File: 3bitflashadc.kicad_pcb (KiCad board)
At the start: 2 copper layers, 118.1 x 88.9 mm, 42 parts, among them J1 ExternalPower, U1 LM339, U2 LM339, U3 LM339, U4 74LS04, U5 7447, U6 74147

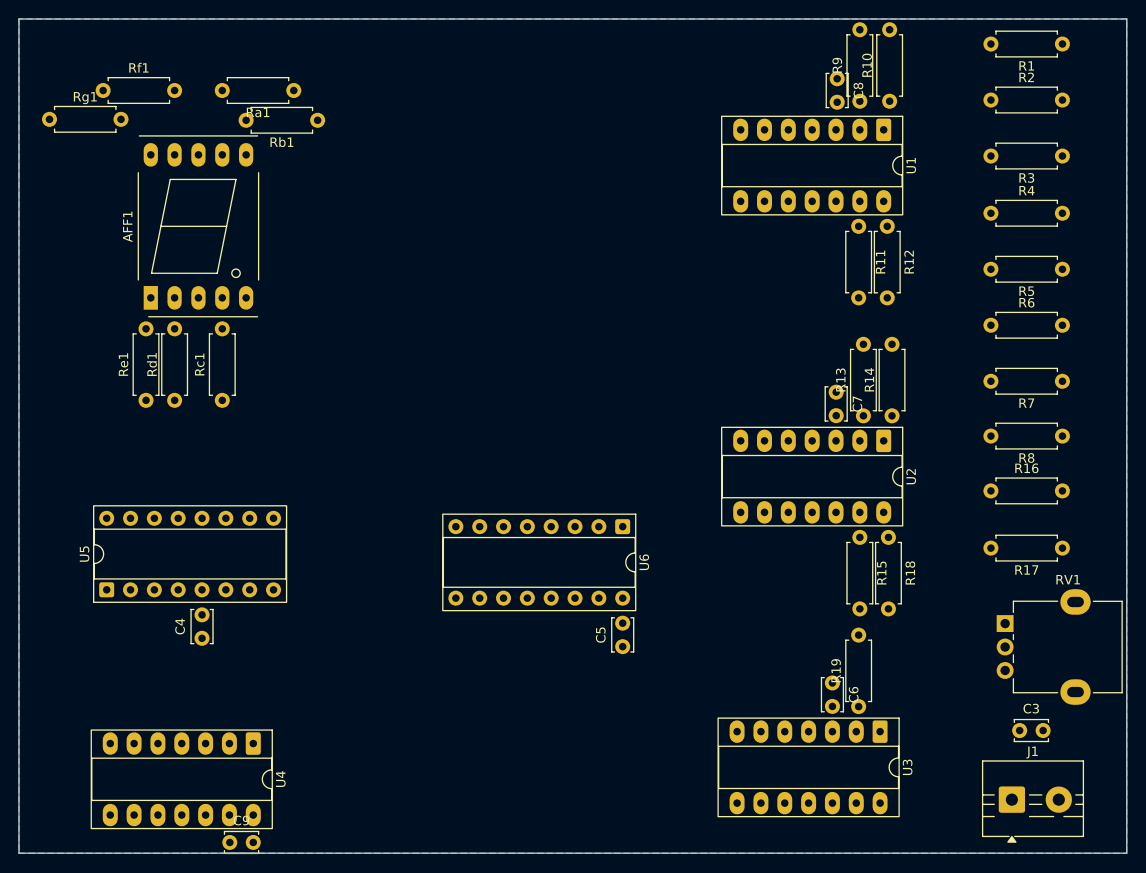
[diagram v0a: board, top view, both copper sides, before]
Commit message: PCB routed except ground (some are needed to be jumpered)
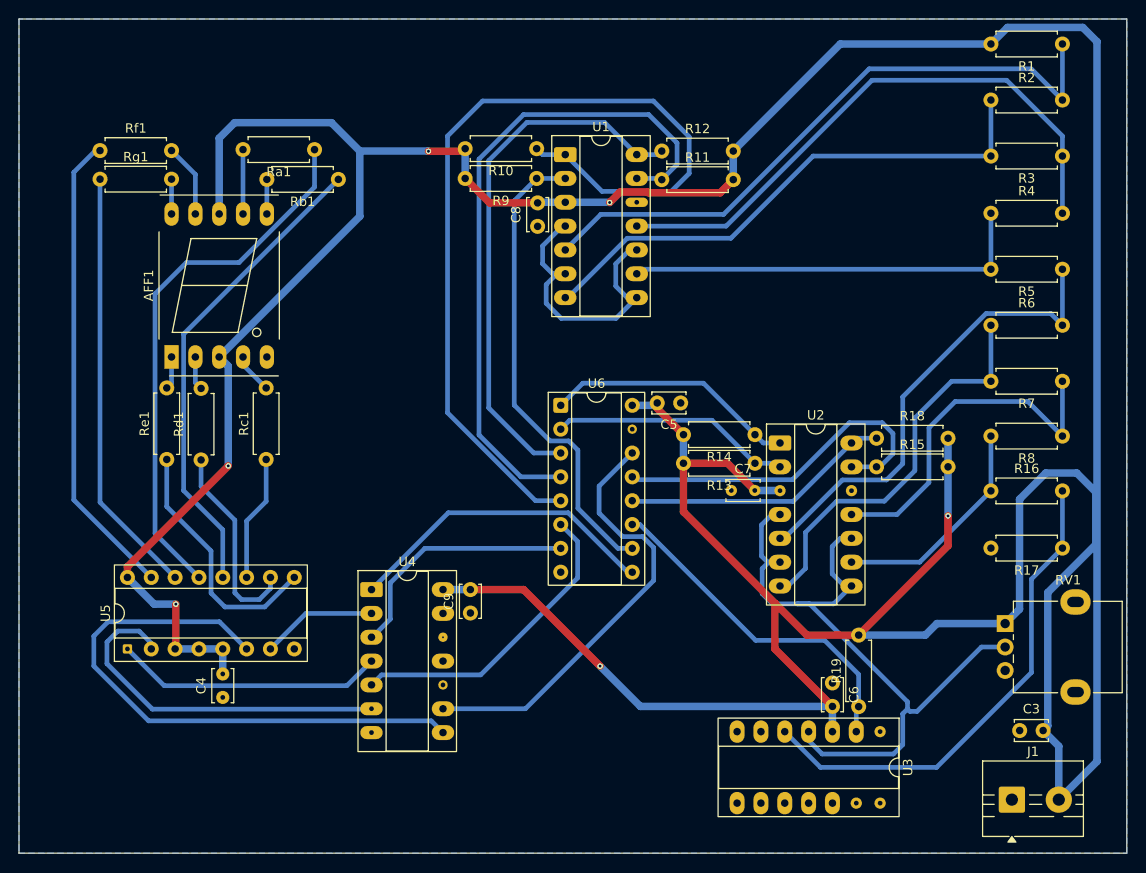
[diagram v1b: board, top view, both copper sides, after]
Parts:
- moved R10 38.0 mm to (144.6, 56.1), turned to 180 degrees
- moved C8 35.6 mm to (144.7, 64.4), turned to 90 degrees
- moved C9 35.4 mm to (137.6, 105.6), turned to 90 degrees
- moved R9 35.4 mm to (144.6, 59.3), turned to 180 degrees
- moved U1 34.0 mm to (147.7, 56.7), turned to 0 degrees
- moved C5 26.7 mm to (160.0, 83.2), turned to 180 degrees
- moved R12 25.3 mm to (158.0, 56.4), turned to 0 degrees
- moved R11 21.6 mm to (158.0, 59.4), turned to 0 degrees
- moved U4 20.7 mm to (127.0, 103.1), turned to 0 degrees
- moved C7 15.3 mm to (165.4, 92.5), turned to 0 degrees
- moved R14 14.7 mm to (167.9, 86.6), turned to 180 degrees
- moved U6 14.5 mm to (147.2, 83.5), turned to 0 degrees
- moved R13 12.6 mm to (167.9, 89.6), turned to 180 degrees
- moved U2 11.1 mm to (170.6, 87.5), turned to 0 degrees
- moved R18 10.6 mm to (180.8, 87.0), turned to 0 degrees
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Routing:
- net 5V: track 0.00 -> 490.9 mm, vias 0 -> 6
- net Net-(U1A--): track 0.00 -> 109.5 mm
- net 1B: track 0.00 -> 97.2 mm
- net 1C: track 0.00 -> 71.6 mm
- net Net-(U1A-+): track 0.00 -> 68.3 mm
- net Net-(U1C-+): track 0.00 -> 62.5 mm
- net D: track 0.00 -> 61.5 mm
- net Net-(U5-~{a}): track 0.00 -> 57.9 mm
- net 1D: track 0.00 -> 57.7 mm
- net Net-(U1B-+): track 0.00 -> 57.6 mm
- net Net-(U3A-+): track 0.00 -> 52.8 mm
- net Net-(U5-~{b}): track 0.00 -> 51.0 mm
- net 1A: track 0.00 -> 50.7 mm
- net Net-(U2A-+): track 0.00 -> 50.7 mm
- net Net-(U5-~{f}): track 0.00 -> 50.4 mm
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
